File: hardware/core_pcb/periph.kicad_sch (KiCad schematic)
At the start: 17 parts, among them J4 RVT70 RiBUS, U8 W25Q128JV, U9 MB85RC1MT

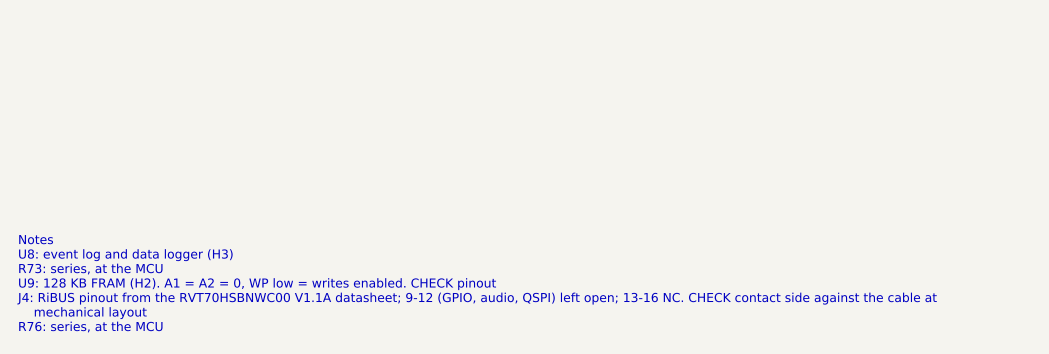
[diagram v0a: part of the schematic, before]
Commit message: Core PCB: save datasheets and clear the datasheet checks
Add hardware/datasheets with the six datasheets Gary supplied and an index.
Apply what they show: TPS54360B with 22 uH and compensation from its
datasheet, LAN8742A crystal caps 33 pF, W5500 reserved pins 38-42 left open
and its reference crystal circuit (1M, 0R), FRAM and choke checks cleared.

Co-Authored-By: Claude Opus 5.5 (1M context) <noreply@anthropic.com>
Claude-Session: https://claude.ai/code/session_014onnq3eRiDkqdAB6fKiRDW
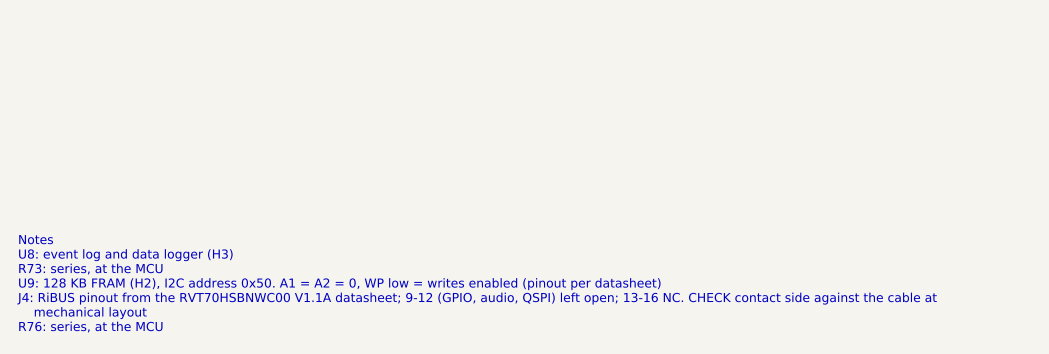
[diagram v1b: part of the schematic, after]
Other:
- note added: "Notes U8: event log and data logger (H3) R73: series, at the MCU U9: 128 KB FRAM (H2), I2C address 0x50. A1 = A2 = 0, WP low = writes enabled (pinout per datasheet) J4: RiBUS pinout from the RVT70HSBNWC00 V1.1A datasheet; 9-12 (GPIO, audio, QSPI) left open; 13-16 NC. CHECK contact side against the cable at mechanical layout R76: series, at the MCU"
- note removed: "Notes U8: event log and data logger (H3) R73: series, at the MCU U9: 128 KB FRAM (H2). A1 = A2 = 0, WP low = writes enabled. CHECK pinout J4: RiBUS pinout from the RVT70HSBNWC00 V1.1A datasheet; 9-12 (GPIO, audio, QSPI) left open; 13-16 NC. CHECK contact side against the cable at mechanical layout R76: series, at the MCU"
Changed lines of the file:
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@@
   (no_connect (at 205.73999999999998 58.42))
   (no_connect (at 205.73999999999998 40.64))
-  (text "Notes\nU8: event log and data logger (H3)\nR73: series, at the MCU\nU9: 128 KB FRAM (H2). A1 = A2 = 0, WP low = writes enabled. CHECK pinout\nJ4: RiBUS pinout from the RVT70HSBNWC00 V1.1A datasheet; 9-12 (GPIO, audio, QSPI) left open; 13-16 NC. CHECK contact side against the cable at\n    mechanical layout\nR76: series, at the MCU"
+  (text "Notes\nU8: event log and data logger (H3)\nR73: series, at the MCU\nU9: 128 KB FRAM (H2), I2C address 0x50. A1 = A2 = 0, WP low = writes enabled (pinout per datasheet)\nJ4: RiBUS pinout from the RVT70HSBNWC00 V1.1A datasheet; 9-12 (GPIO, audio, QSPI) left open; 13-16 NC. CHECK contact side against the cable at\n    mechanical layout\nR76: series, at the MCU"
     (at 15.24 137.16 0)
     (effects (font (size 1.0 1.0)) (justify left top))

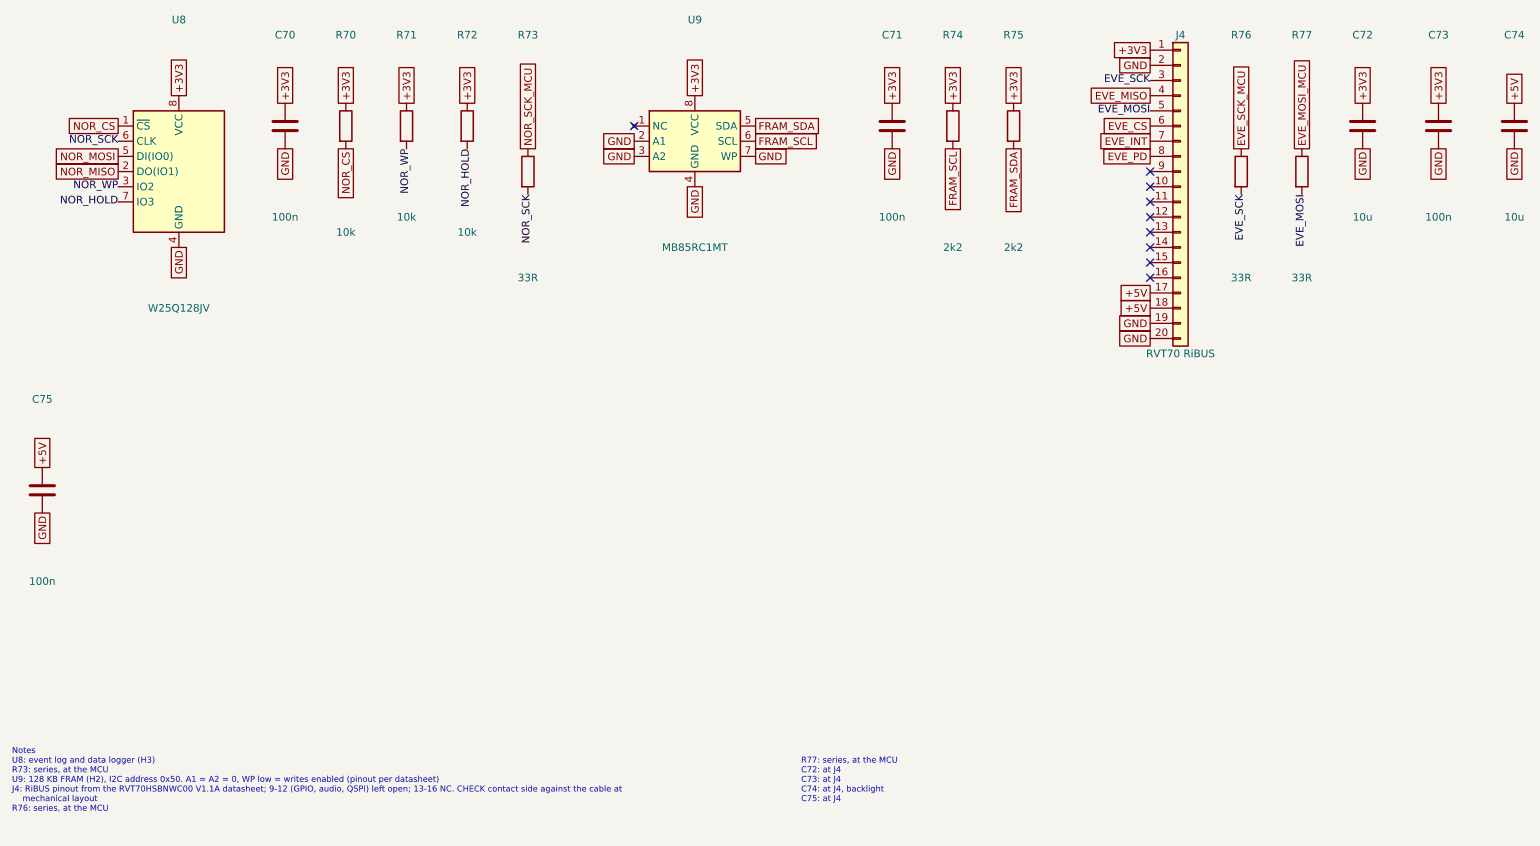
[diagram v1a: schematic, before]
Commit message: Core PCB: add the 8 MB QSPI PSRAM (APS6404L) on OCTOSPI1
Gary approved the PSRAM (29 Oct) for working RAM headroom. U10 on PB2 CLK,
PB10 NCS, PB1/PB0/PC2/PA6 IO0-3 (pins agreed with the RAM thread, all
previously free), 33R series on CLK, 10k pull-up on NCS, 100n + 1u.
Project symbol APS6404L derived from KiCad's ESP-PSRAM32 (same pinout).

Co-Authored-By: Claude Opus 5.5 <noreply@anthropic.com>
Claude-Session: https://claude.ai/code/session_014onnq3eRiDkqdAB6fKiRDW
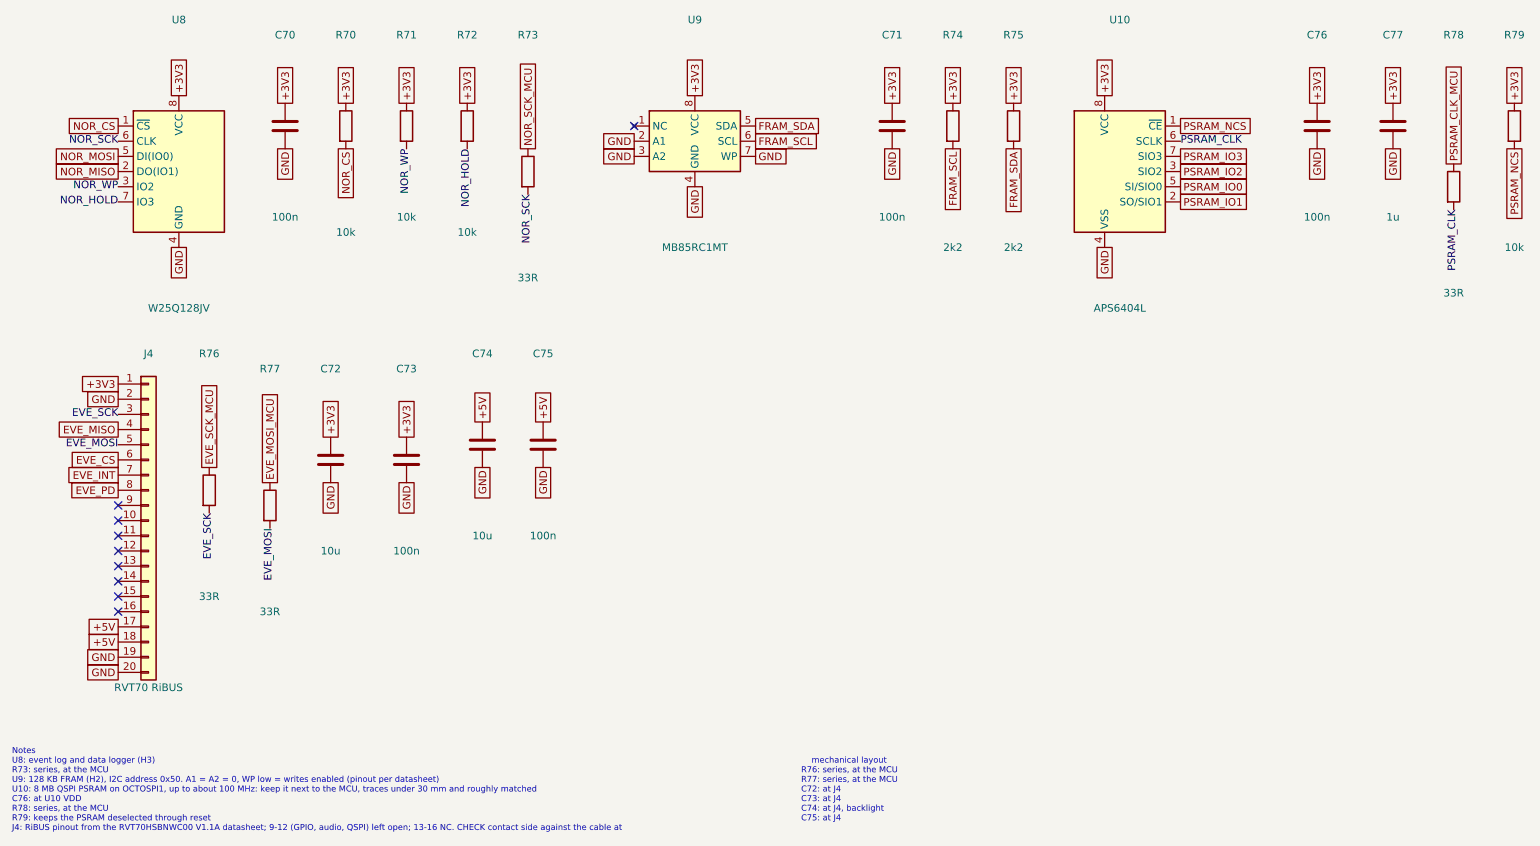
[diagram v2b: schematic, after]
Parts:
- added C76: 100n, Capacitor_SMD:C_0603_1608Metric, symbol Device:C
- added C77: 1u, Capacitor_SMD:C_0603_1608Metric, symbol Device:C
- added R78: 33R, Resistor_SMD:R_0603_1608Metric, symbol Device:R
- added R79: 10k, Resistor_SMD:R_0603_1608Metric, symbol Device:R
- added U10: APS6404L, Package_SO:SOIC-8_3.9x4.9mm_P1.27mm, symbol cems_core:APS6404L
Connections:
- net +3V3: now also C76.1, C77.1, R79.1, U10.8 (VCC)
- net GND: now also C76.2, C77.2, U10.4 (VSS)
- new net PSRAM_CLK: R78.2, U10.6 (SCLK)
- new net PSRAM_CLK_MCU: R78.1
- new net PSRAM_IO0: U10.5 (SI/SIO0)
- new net PSRAM_IO1: U10.2 (SO/SIO1)
- new net PSRAM_IO2: U10.3 (SIO2)
- new net PSRAM_IO3: U10.7 (SIO3)
- new net PSRAM_NCS: R79.2, U10.1 (~{CE})
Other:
- note added: "Notes U8: event log and data logger (H3) R73: series, at the MCU U9: 128 KB FRAM (H2), I2C address 0x50. A1 = A2 = 0, WP low = writes enabled (pinout per datasheet) U10: 8 MB QSPI PSRAM on OCTOSPI1, up to about 100 MHz: keep it next to the MCU, traces under 30 mm and roughly matched C76: at U10 VDD R78: series, at the MCU R79: keeps the PSRAM deselected through reset J4: RiBUS pinout from the RVT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"
- note added: "mechanical layout R76: series, at the MCU R77: series, at the MCU C72: at J4 C73: at J4 C74: at J4, backlight C75: at J4"
- note removed: "Notes U8: event log and data logger (H3) R73: series, at the MCU U9: 128 KB FRAM (H2), I2C address 0x50. A1 = A2 = 0, WP low = writes enabled (pinout per datasheet) J4: RiBUS pinout from the RVT70HSBNWC00 V1.1A datasheet; 9-12 (GPIO, audio, QSPI) left open; 13-16 NC. CHECK contact side against the cable at mechanical layout R76: series, at the MCU"
- note removed: "R77: series, at the MCU C72: at J4 C73: at J4 C74: at J4, backlight C75: at J4"
- moved on the sheet: C72, C73, C74, C75, J4, R76, R77
